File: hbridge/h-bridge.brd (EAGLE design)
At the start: 44.5 x 44.5 mm, 7 parts

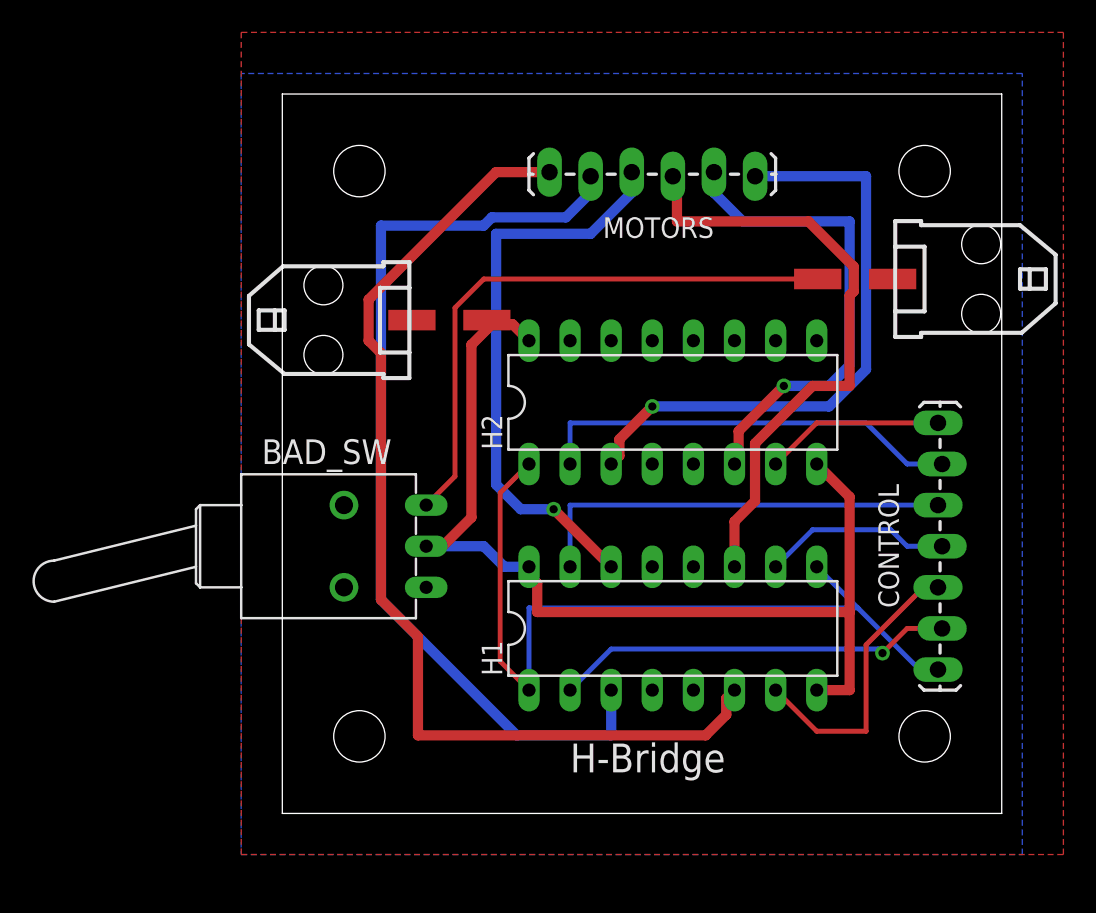
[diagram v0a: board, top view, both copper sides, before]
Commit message: Rework H-bridge to add charge port, move headers to back
- correct hole sizes and placement
- added key dimension documentation
- switch toggles battery between circuit and charge port
- headers on backside leading toward center of chassis
- battery in and daisy chain output also point into center
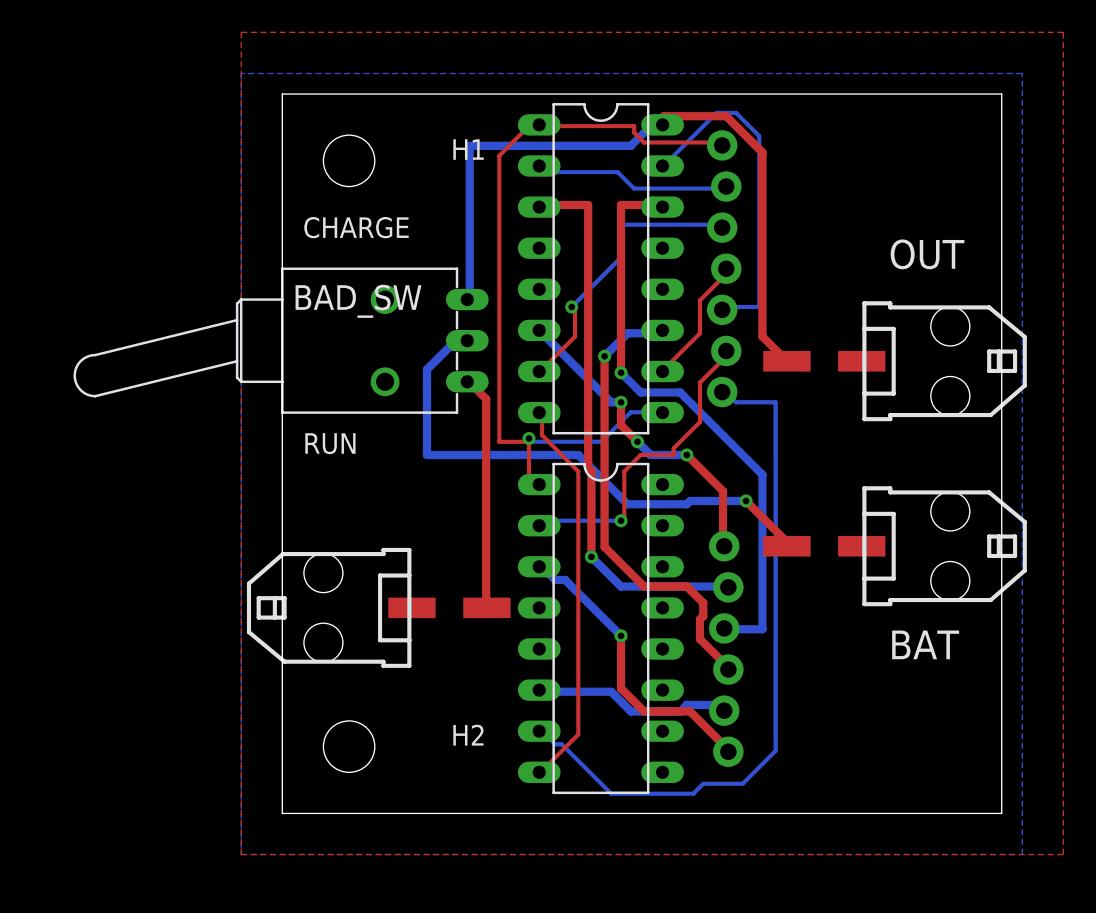
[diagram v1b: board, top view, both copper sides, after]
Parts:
- removed VIN, VOUT: (no value), con-molex-micro-fit-3_0:43045-0206
- added BAT, CHARGE, OUT: (no value), con-molex-micro-fit-3_0:43045-0206
- CONTROL: device SparkFun-Connectors:1X07_LOCK_LONGPADS -> SparkFun-Connectors:1X07_LOCK
- MOTORS: device SparkFun-Connectors:1X06_LOCK_LONGPADS -> SparkFun-Connectors:1X06_LOCK
- moved CONTROL 35.0 mm to (27.3, 41.3), flipped to the bottom, turned to 270 degrees
- moved MOTORS 22.9 mm to (27.3, 16.5), flipped to the bottom, turned to 270 degrees
- moved H1 22.7 mm to (19.7, 33.7), turned to 270 degrees
- moved H2 14.7 mm to (19.7, 11.4), turned to 270 degrees
- moved BAD_SW 13.0 mm to (6.35, 29.2)
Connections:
- removed net N$3: BAD_SW.3, VOUT.P$2
- new net VCC1: H2.16
- new net VCC2: H1.8, H2.8
- new net V_CHARGE: BAD_SW.1, CHARGE.P$2
- new net V_RUN: BAD_SW.3, H1.16, OUT.P$2
- net GND: now also BAT.P$1, CHARGE.P$1, OUT.P$1; no longer VIN.P$1, VOUT.P$1
- net M1+: now also MOTORS.1; no longer MOTORS.6
- net M1-: now also MOTORS.2; no longer MOTORS.5
- net M2+: now also MOTORS.3; no longer MOTORS.4
- net M2-: now also MOTORS.4; no longer MOTORS.3
- net M3+: now also MOTORS.5; no longer MOTORS.2
- net M3-: now also MOTORS.6; no longer MOTORS.1
- net V+: now also BAT.P$2; no longer H1.16, H1.8, H2.16, H2.8, VIN.P$2
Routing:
- net M1+: track 63.9 -> 19.7 mm, vias 0 -> 3
- net V_RUN: track 0.00 -> 43.1 mm
- net N$3: track 36.1 -> 0.00 mm
- net V+: track 65.4 -> 33.4 mm, vias 0 -> 1
- net M3_DIR: track 11.1 -> 42.4 mm
- net M1-: track 58.4 -> 34.1 mm, vias 0 -> 1
- net VCC2: track 0.00 -> 24.3 mm
- net M3-: track 37.6 -> 18.4 mm
- net M3+: track 30.0 -> 12.3 mm, vias 1 -> 0
- net V_CHARGE: track 0.00 -> 14.5 mm
- net M1_MOVE: track 24.8 -> 12.3 mm, vias 1 -> 0
- net M2-: track 37.9 -> 28.5 mm, vias 0 -> 1
- net M3_MOVE: track 26.6 -> 19.5 mm, vias 0 -> 1
- net M2_DIR: track 26.5 -> 20.9 mm
- net ENABLE: track 51.0 -> 47.1 mm, vias 0 -> 1
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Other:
- board text added: "BAT"
- board text added: "CHARGE"
- board text added: "D1"
- board text added: "D2"
- board text added: "D3"
- board text added: "En"
- board text added: "M1"
- board text added: "M1+"
- board text added: "M1-"
- board text added: "M2"
- board text added: "M2+"
- board text added: "M2-"
- board text added: "M3"
- board text added: "M3+"
- board text added: "M3-"
- board text added: "OUT"
- board text added: "RUN"
- board text removed: "H-Bridge"

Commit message: Fix V_RUN net so that it is actually attached to ICs
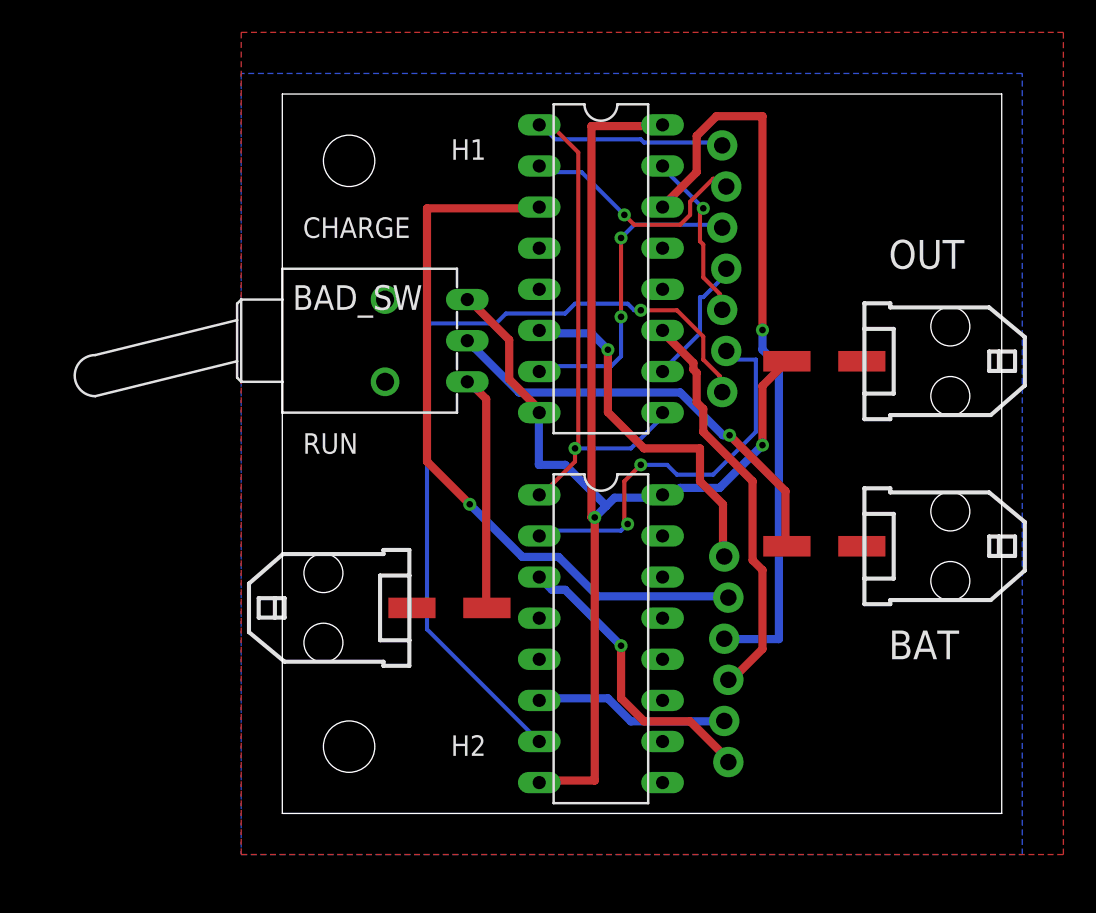
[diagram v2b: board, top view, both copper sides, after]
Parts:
- moved MOTORS 0.64 mm to (27.3, 15.9)
- moved H2 0.63 mm to (19.7, 10.8)
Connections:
- removed net VCC1: H2.16
- removed net VCC2: H1.8, H2.8
- net V_RUN: now also H1.8, H2.16, H2.8
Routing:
- net V_RUN: track 43.1 -> 83.9 mm, vias 0 -> 2
- net VCC2: track 24.3 -> 0.00 mm
- net M1-: track 34.1 -> 44.7 mm
- net M2_DIR: track 20.9 -> 10.6 mm, vias 0 -> 1
- net M2+: track 36.3 -> 45.9 mm
- net M3_DIR: track 42.4 -> 51.0 mm, vias 0 -> 1
- net V+: track 33.4 -> 26.9 mm
- net M3_MOVE: track 19.5 -> 25.0 mm, vias 1 -> 2
- net ENABLE: track 47.1 -> 43.7 mm
- net M2-: track 28.5 -> 25.2 mm, vias 1 -> 0
- net M1_MOVE: track 12.3 -> 15.2 mm, vias 0 -> 1
- net M1+: track 19.7 -> 22.5 mm, vias 3 -> 1
- net M1_DIR: track 17.7 -> 19.4 mm, vias 1 -> 2

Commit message: Update H-bridge board to use correct switch
- The E-switch WSP1 is a custom model from the wolfbot.lbr library
- Shifted most components due to the larger switch footprint
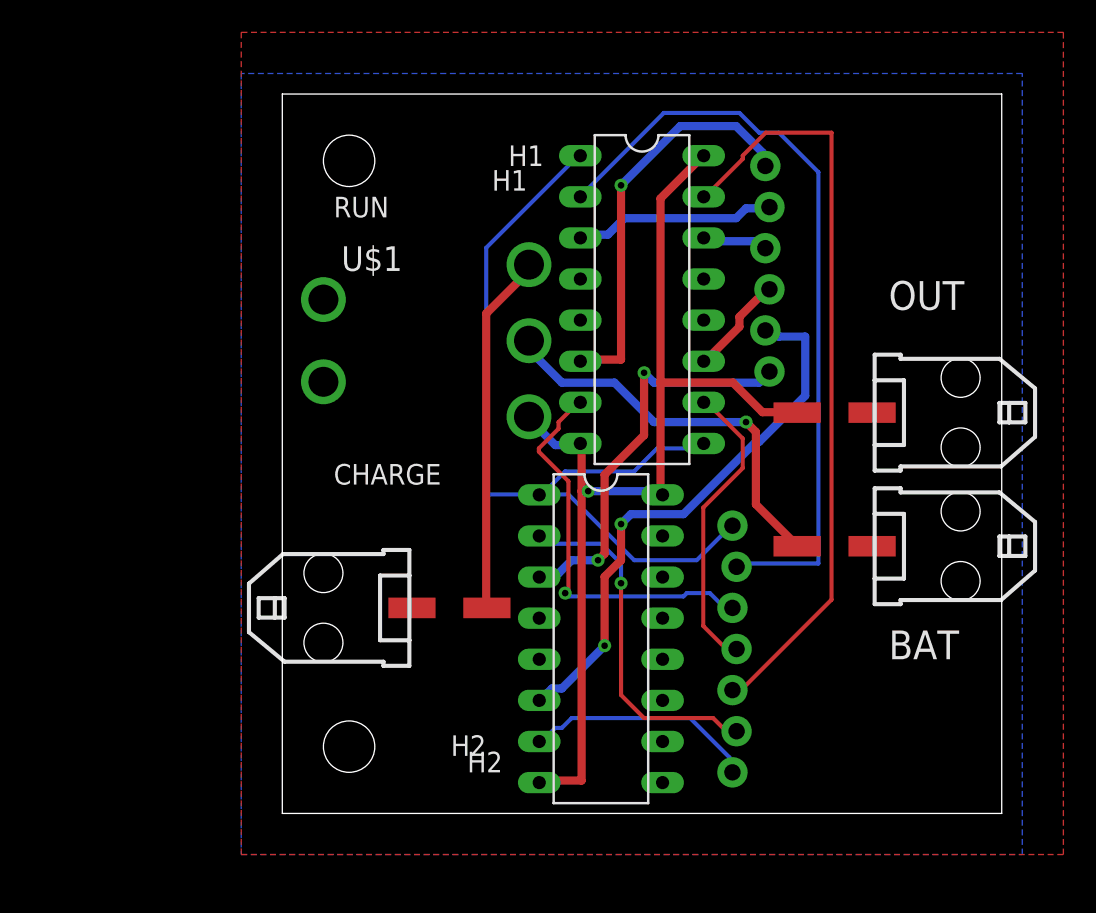
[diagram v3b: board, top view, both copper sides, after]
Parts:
- removed BAD_SW: (no value), switch:9070-1W
- added U$1: ESWITCH-WSP1, wolfbot:WSP1-T2-M6
- moved MOTORS 24.3 mm to (29.8, 40.0)
- moved CONTROL 23.5 mm to (27.9, 17.8)
- moved OUT 3.24 mm to (41.9, 24.8)
- moved H1 3.18 mm to (22.2, 31.8)
- moved BAT 0.63 mm to (41.9, 16.5)
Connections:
- net GND: no longer BAD_SW.B, BAD_SW.B1
- net V+: now also U$1.2; no longer BAD_SW.2
- net V_CHARGE: now also U$1.3; no longer BAD_SW.1
- net V_RUN: now also U$1.1; no longer BAD_SW.3
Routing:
- net M2+: track 45.9 -> 4.06 mm, vias 1 -> 0
- net M3_DIR: track 51.0 -> 14.4 mm, vias 1 -> 0
- net M2_DIR: track 10.6 -> 47.0 mm, vias 1 -> 0
- net M1_MOVE: track 15.2 -> 47.7 mm, vias 1 -> 0
- net M1-: track 44.7 -> 12.5 mm, vias 1 -> 0
- net M3+: track 12.1 -> 34.4 mm, vias 0 -> 2
- net V_RUN: track 83.9 -> 64.0 mm, vias 2 -> 1
- net M2-: track 25.2 -> 6.40 mm
- net M2_MOVE: track 8.09 -> 18.6 mm
- net ENABLE: track 43.7 -> 52.5 mm, vias 1 -> 0
- net V_CHARGE: track 14.5 -> 22.3 mm
- net M3-: track 18.4 -> 25.1 mm, vias 1 -> 2
- net M1_DIR: track 19.4 -> 24.6 mm, vias 2 -> 1
- net M3_MOVE: track 25.0 -> 21.9 mm, vias 2 -> 1
- net M1+: track 22.5 -> 25.3 mm
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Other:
- board text added: "H1"
- board text added: "H2"

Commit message: Reroute H-bridge board for conservative design rules
- 20 mil drill holes
- 20 mil power traces with 20 mil clearance
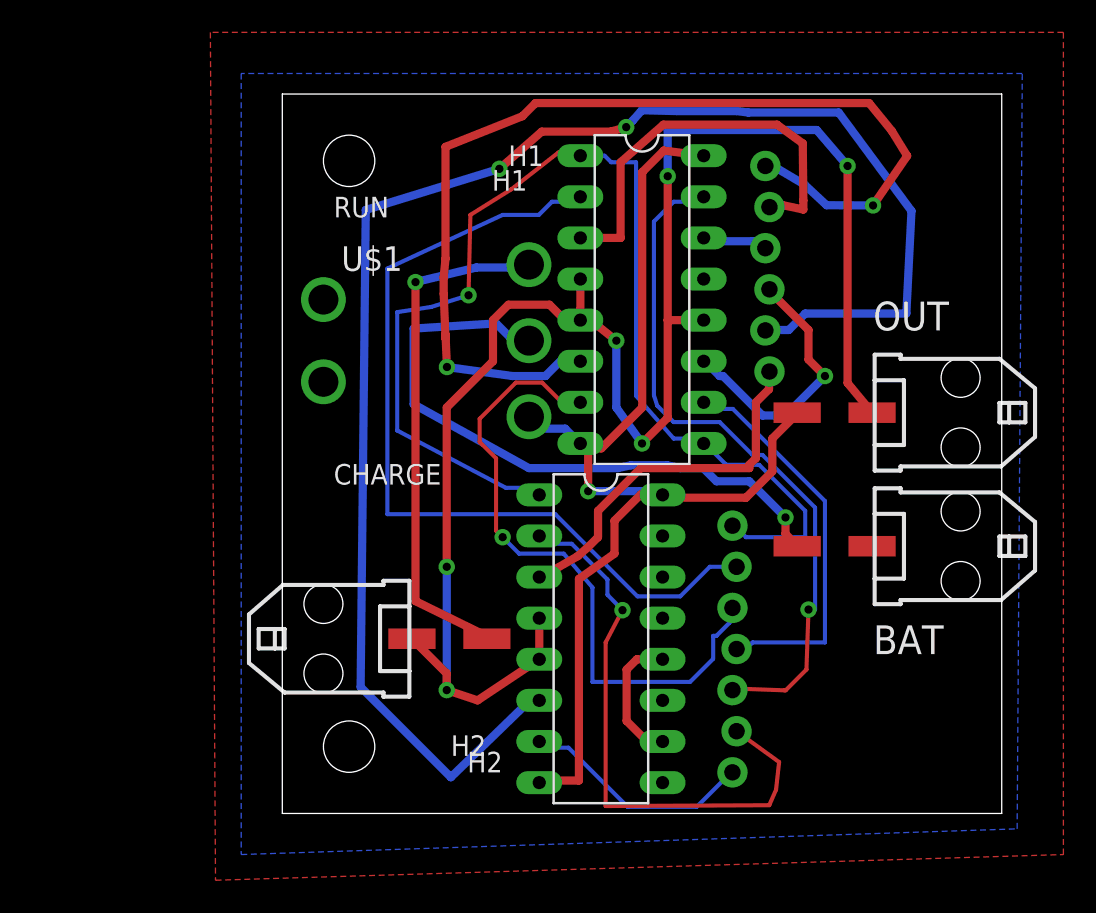
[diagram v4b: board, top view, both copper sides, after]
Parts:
- moved CHARGE 1.90 mm to (2.54, 10.8)
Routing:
- net GND: track 0.00 -> 114.3 mm, vias 0 -> 6
- net M3+: track 34.4 -> 99.1 mm
- net M1+: track 25.3 -> 64.9 mm, vias 1 -> 2
- net ENABLE: track 52.5 -> 72.9 mm, vias 0 -> 1
- net M1_DIR: track 24.6 -> 40.2 mm
- net V+: track 24.8 -> 39.6 mm
- net M3_MOVE: track 21.9 -> 36.1 mm
- net M1-: track 12.5 -> 25.9 mm
- net M2-: track 6.40 -> 16.7 mm, vias 0 -> 1
- net V_CHARGE: track 22.3 -> 32.1 mm, vias 0 -> 1
- net V_RUN: track 64.0 -> 70.9 mm
- net M2_MOVE: track 18.6 -> 24.4 mm
- net M1_MOVE: track 47.7 -> 52.7 mm
- net M2_DIR: track 47.0 -> 43.1 mm, vias 0 -> 1
- net M3-: track 25.1 -> 23.0 mm, vias 2 -> 0
